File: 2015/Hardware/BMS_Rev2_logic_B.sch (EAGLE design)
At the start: 38 parts, among them Q9 MOSFET-NCHANNEL2N7002PW

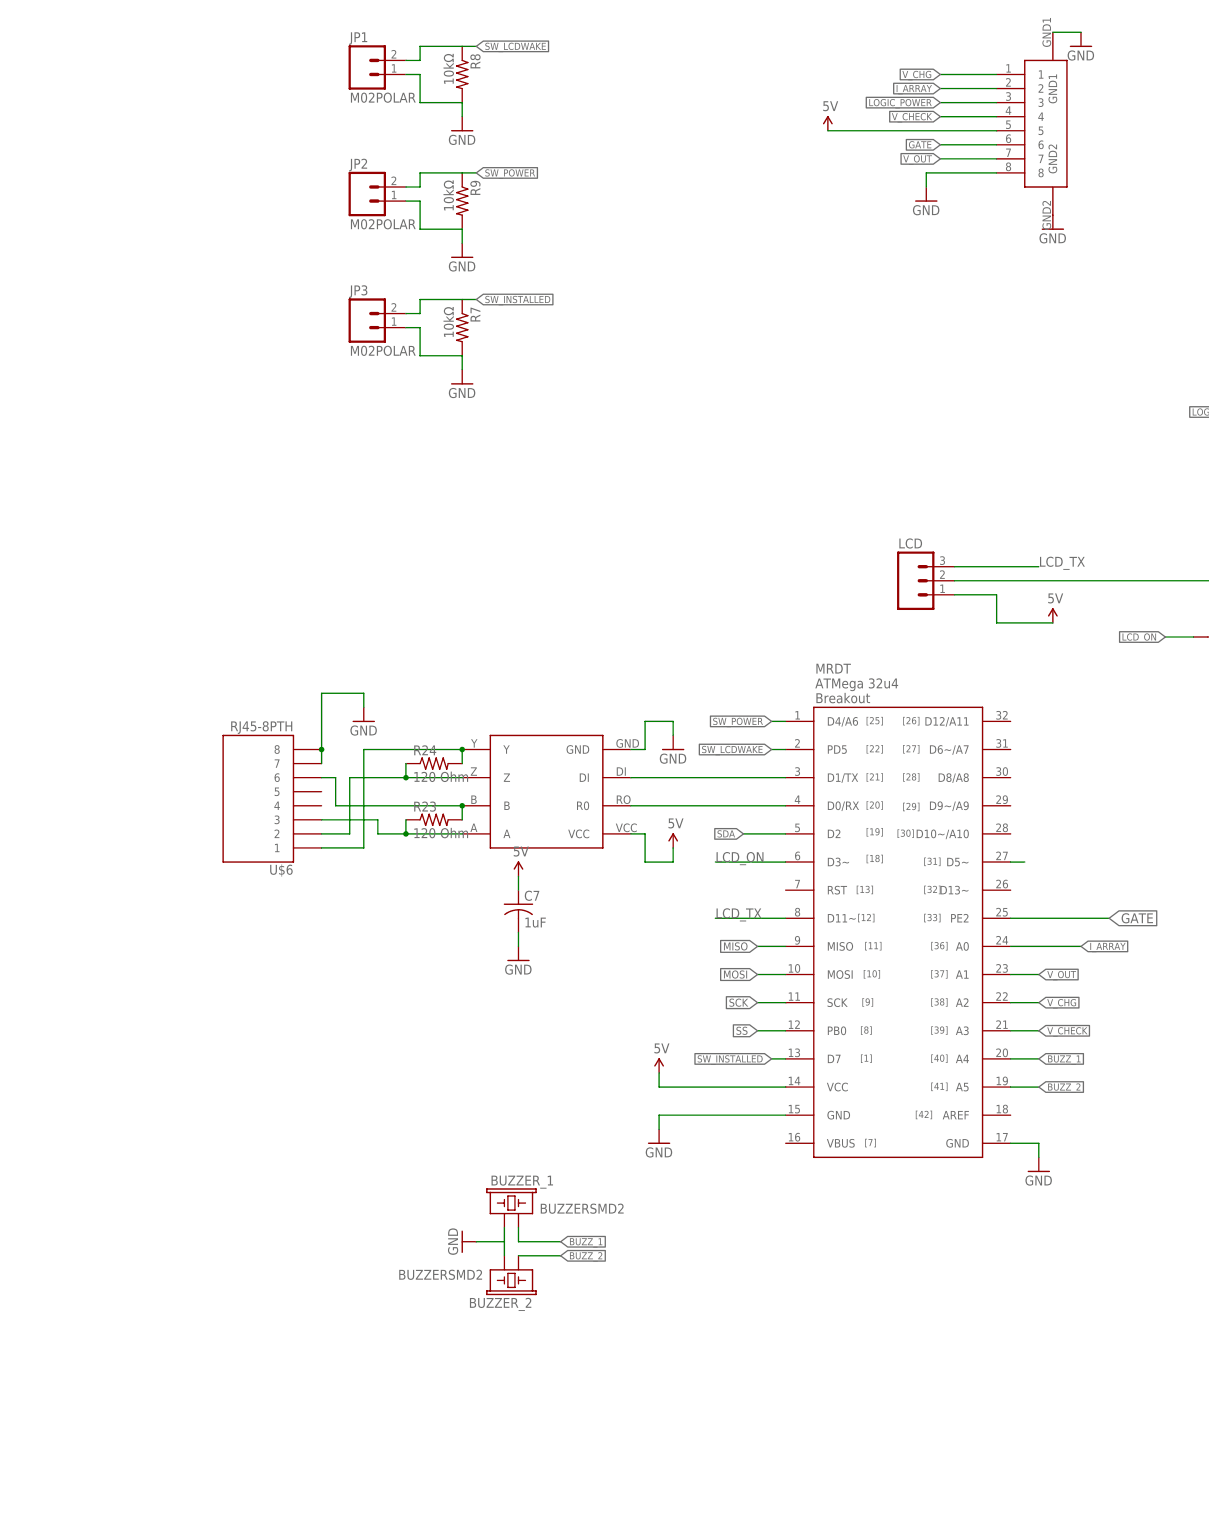
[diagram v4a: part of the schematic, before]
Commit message: BMS Revision C
Fixed minor problems with the logic board.
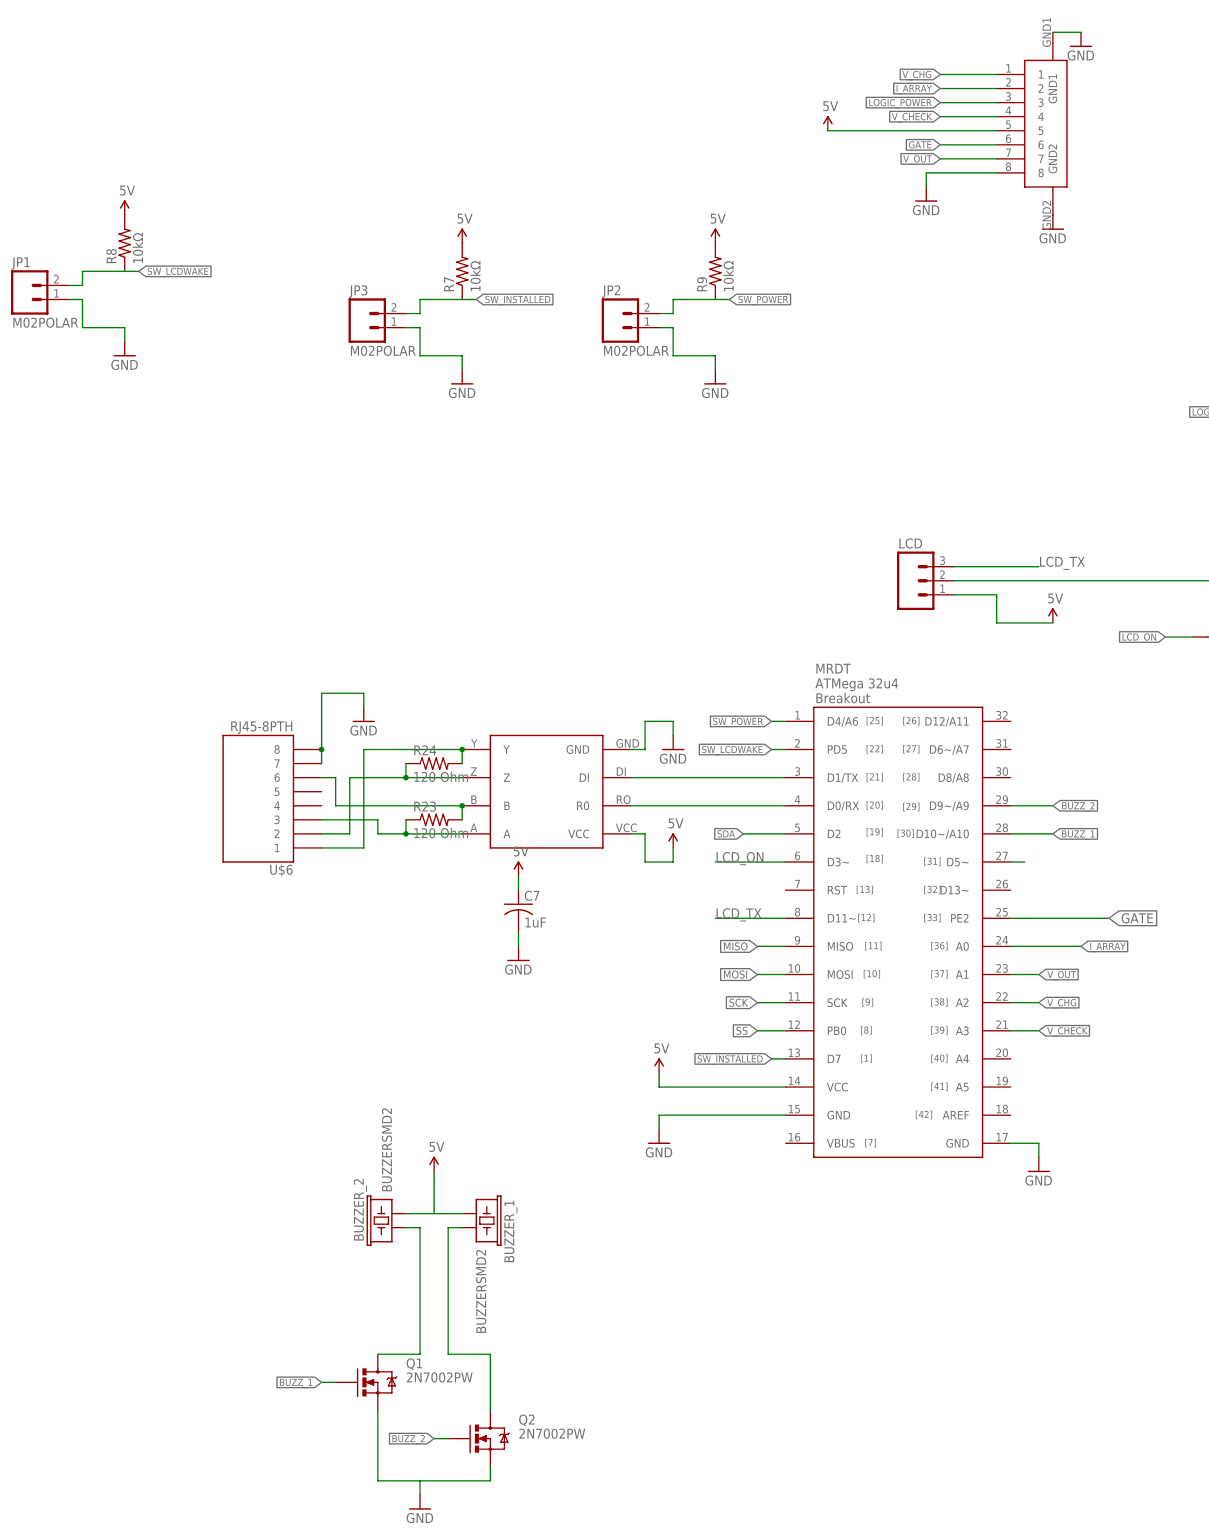
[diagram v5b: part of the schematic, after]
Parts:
- added Q1, Q2: 2N7002PW, SparkFun-DiscreteSemi:MOSFET-NCHANNEL2N7002PW
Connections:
- new net N$19: BUZZER_2.1, Q1.D
- new net N$8: BUZZER_1.2, Q2.D
- net 5V: now also BUZZER_1.1, BUZZER_2.2, R7.2, R8.2, R9.2
- net BUZZ_1: now also Q1.G, U$3.D10~/A10; no longer BUZZER_1.2, U$3.A4
- net BUZZ_2: now also Q2.G, U$3.D9~/A9; no longer BUZZER_2.1, U$3.A5
- net GND: now also Q1.S, Q2.S; no longer BUZZER_1.1, BUZZER_2.2, R7.2, R8.2, R9.2
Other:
- moved on the sheet: BUZZER_1, BUZZER_2, JP1, JP2, R7, R8, R9
